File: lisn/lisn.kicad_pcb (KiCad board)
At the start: 2 copper layers, 50 x 49 mm, 33 parts, among them J1 IN+, J2 IN-, J3 GND, J4 GND, J5 OUT+, J6 OUT-, J7 SMA, SW1 DPDT, T1 SWB2010

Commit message: Update LISN PCB
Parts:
- added R9: 68, Resistor_SMD:R_0603_1608Metric, F.Cu at (160.6, 99.2)
- R5, R6: value 50 -> 82
- R7: value 18 -> 30
- R8: value 82 -> 68
- moved R8 27.1 mm to (164.7, 99.2)
- moved R3 4.33 mm to (167.3, 98.0)
- moved R4 4.33 mm to (168.8, 98.0)
- moved R1 2.55 mm to (156.5, 98.0)
- moved R2 2.55 mm to (158.0, 98.0)
- moved C4 2.50 mm to (160.5, 96.0), turned to -90 degrees
- moved C5 2.09 mm to (164.8, 96.0), turned to -90 degrees
- moved R7 1.43 mm to (137.8, 107.4)
- moved D1 1.10 mm to (158.7, 102.5)
- moved D2 1.04 mm to (161.1, 102.5)
- moved D3 0.99 mm to (163.5, 102.5)
- moved D4 0.94 mm to (165.9, 102.5)
- moved R5 0.10 mm to (154.1, 103.2)
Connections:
- R8 pad 1: GND -> Net-(D3-K)
- R8 pad 2: Net-(D5-A) -> GND
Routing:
- net GND: track 87.4 -> 134.3 mm
- net Net-(D3-K): track 18.9 -> 24.8 mm
- net Net-(D5-A): track 13.4 -> 10.3 mm
- net Net-(D1-K): track 16.4 -> 18.8 mm
- net Net-(C4-Pad2): track 5.27 -> 4.12 mm
- net /OUT_M: track 16.5 -> 17.6 mm
- net /OUTPUT: track 23.7 -> 24.6 mm

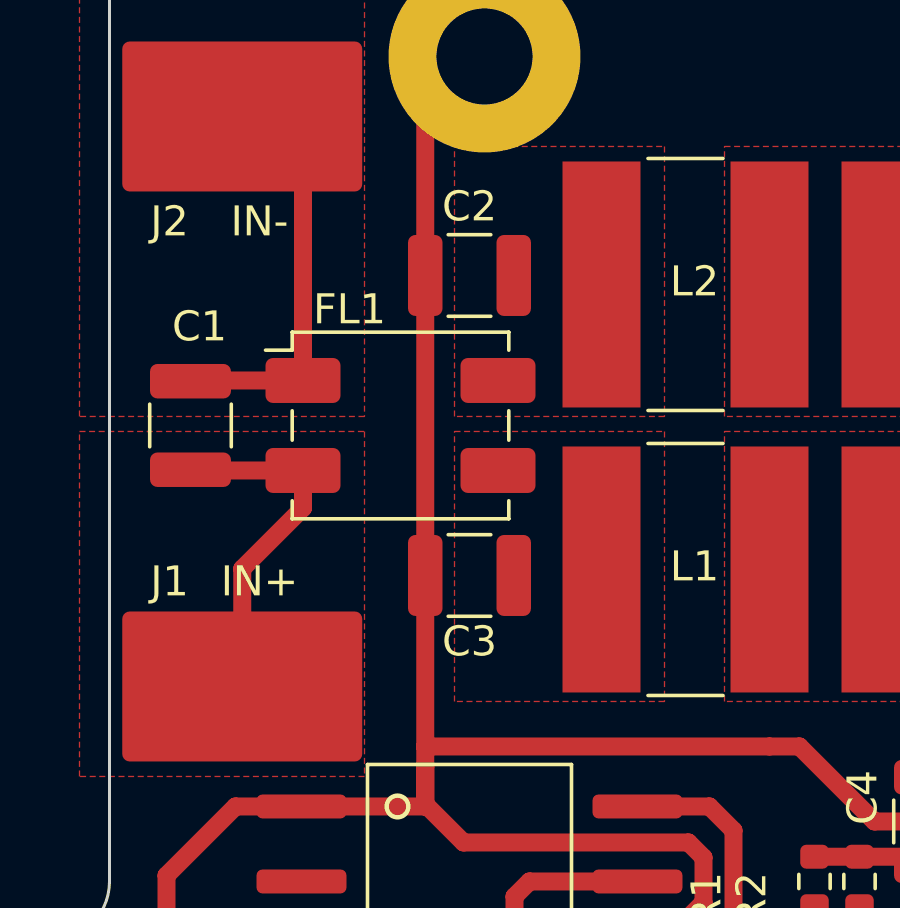
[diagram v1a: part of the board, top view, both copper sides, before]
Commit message: Add parametric FreeCAD design, add README.
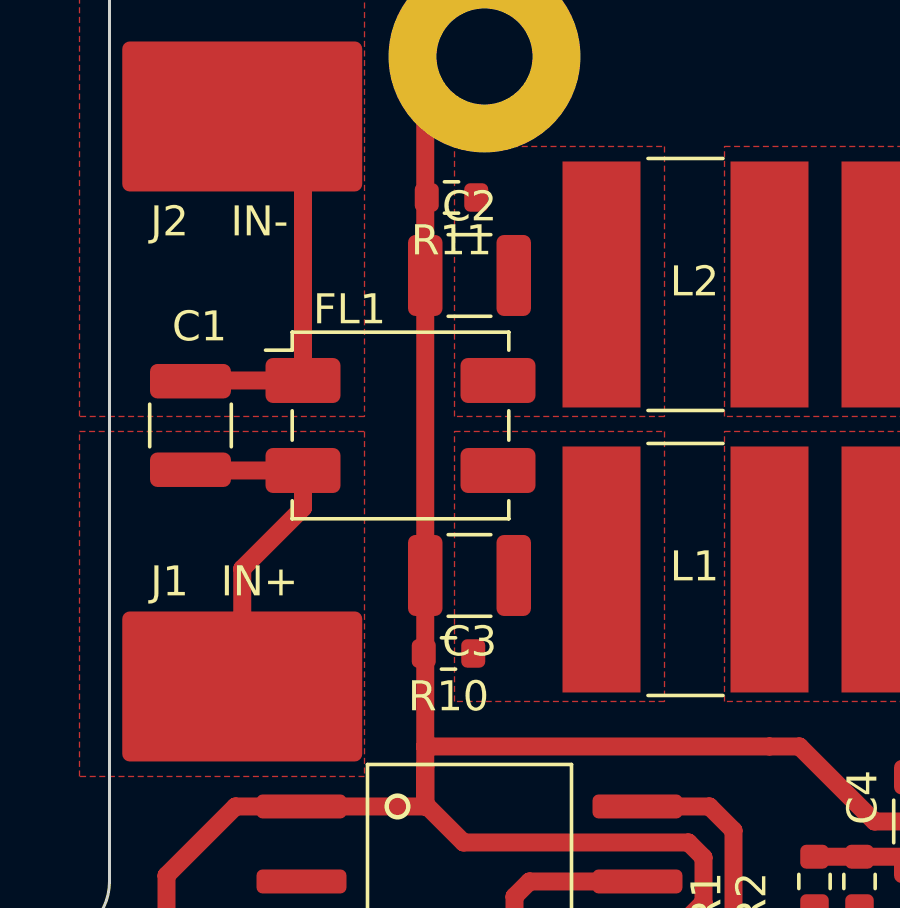
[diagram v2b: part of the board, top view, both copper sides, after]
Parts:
- added R10: 100k, Resistor_SMD:R_0603_1608Metric, F.Cu at (144.3, 90.4)
- added R11: 100k, Resistor_SMD:R_0603_1608Metric, F.Cu at (144.4, 75.2)
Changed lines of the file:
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@@
+  )
+  (footprint "Resistor_SMD:R_0603_1608Metric" (layer "F.Cu")
+    (at 144.3 90.4 180)
+    (descr "Resistor SMD 0603 (1608 Metric), square (rectangular) end terminal, IPC_7351 nominal, (Body size source: IPC-SM-782 page 72, https://www.pcb-3d.com/wordpress/wp-content/uploads/ipc-sm-782a_amendment_1_and_2.pdf), generated with kicad-footprint-generator")
+    (tags "resistor")
+    (property "Sheetfile" "lisn.kicad_sch")
+    (property "Sheetname" "")
+    (property "ki_description" "Resistor")
+    (property "ki_keywords" "R res resistor")
+    (attr smd)
+    (fp_text reference "R10" (at 0 -1.43) (layer "F.SilkS")
+        (effects (font (size 1 1) (thickness 0.15)))
+    )
+    (fp_text value "100k" (at 0 1.43) (layer "F.Fab")
+        (effects (font (size 1 1) (thickness 0.15)))
+    )
+    (fp_text user "${REFERENCE}" (at 0 0) (layer "F.Fab")
+        (effects (font (size 0.4 0.4) (thickness 0.06)))
+    )
+    (fp_line (start -0.237258 -0.5225) (end 0.237258 -0.5225)
+      (stroke (width 0.12) (type solid)) (layer "F.SilkS"))
+    (fp_line (start -0.237258 0.5225) (end 0.237258 0.5225)
+      (stroke (width 0.12) (type solid)) (layer "F.SilkS"))
+    (fp_line (start -1.48 -0.73) (end 1.48 -0.73)
+      (stroke (width 0.05) (type solid)) (layer "F.CrtYd"))
+    (fp_line (start -1.48 0.73) (end -1.48 -0.73)
+      (stroke (width 0.05) (type solid)) (layer "F.CrtYd"))
+    (fp_line (start 1.48 -0.73) (end 1.48 0.73)
+      (stroke (width 0.05) (type solid)) (layer "F.CrtYd"))
+    (fp_line (start 1.48 0.73) (end -1.48 0.73)
+      (stroke (width 0.05) (type solid)) (layer "F.CrtYd"))
+    (fp_line (start -0.8 -0.4125) (end 0.8 -0.4125)
+      (stroke (width 0.1) (type solid)) (layer "F.Fab"))
+    (fp_line (start -0.8 0.4125) (end -0.8 -0.4125)
+      (stroke (width 0.1) (type solid)) (layer "F.Fab"))
+    (fp_line (start 0.8 -0.4125) (end 0.8 0.4125)
+      (stroke (width 0.1) (type solid)) (layer "F.Fab"))
+    (fp_line (start 0.8 0.4125) (end -0.8 0.4125)
+      (stroke (width 0.1) (type solid)) (layer "F.Fab"))
+    (pad "1" smd roundrect (at -0.825 0 180) (size 0.8 0.95) (layers "F.Cu" "F.Paste" "F.Mask") (roundrect_rratio 0.25)
+      (net 5 "/INF_P") (pintype "passive"))
+    (pad "2" smd roundrect (at 0.825 0 180) (size 0.8 0.95) (layers "F.Cu" "F.Paste" "F.Mask") (roundrect_rratio 0.25)
+      (net 4 "GND") (pintype "passive"))
+    (model "${KICAD6_3DMODEL_DIR}/Resistor_SMD.3dshapes/R_0603_1608Metric.wrl"
+      (offset (xyz 0 0 0))
+      (scale (xyz 1 1 1))
+      (rotate (xyz 0 0 0))
+    )
   )
   (footprint "Resistor_SMD:R_0603_1608Metric" (layer "F.Cu")
@@
       (offset (xyz 0 0 0))
       (scale (xyz 1 1 1))
+      (rotate (xyz 0 0 0))
+    )
+  )
+  (footprint "Resistor_SMD:R_0603_1608Metric" (layer "F.Cu")
+    (at 144.4 75.2 180)
+    (descr "Resistor SMD 0603 (1608 Metric), square (rectangular) end terminal, IPC_7351 nominal, (Body size source: IPC-SM-782 page 72, https://www.pcb-3d.com/wordpress/wp-content/uploads/ipc-sm-782a_amendment_1_and_2.pdf), generated with kicad-footprint-generator")
+    (tags "resistor")
+    (property "Sheetfile" "lisn.kicad_sch")
+    (property "Sheetname" "")
+    (property "ki_description" "Resistor")
+    (property "ki_keywords" "R res resistor")
+    (attr smd)
+    (fp_text reference "R11" (at 0 -1.43) (layer "F.SilkS")
+        (effects (font (size 1 1) (thickness 0.15)))
+    )
+    (fp_text value "100k" (at 0 1.43) (layer "F.Fab")
+        (effects (font (size 1 1) (thickness 0.15)))
+    )
+    (fp_text user "${REFERENCE}" (at 0 0) (layer "F.Fab")
+        (effects (font (size 0.4 0.4) (thickness 0.06)))
+    )
+    (fp_line (start -0.237258 -0.5225) (end 0.237258 -0.5225)
+      (stroke (width 0.12) (type solid)) (layer "F.SilkS"))
+    (fp_line (start -0.237258 0.5225) (end 0.237258 0.5225)
+      (stroke (width 0.12) (type solid)) (layer "F.SilkS"))
+    (fp_line (start -1.48 -0.73) (end 1.48 -0.73)
+      (stroke (width 0.05) (type solid)) (layer "F.CrtYd"))
+    (fp_line (start -1.48 0.73) (end -1.48 -0.73)
+      (stroke (width 0.05) (type solid)) (layer "F.CrtYd"))
+    (fp_line (start 1.48 -0.73) (end 1.48 0.73)
+      (stroke (width 0.05) (type solid)) (layer "F.CrtYd"))
+    (fp_line (start 1.48 0.73) (end -1.48 0.73)
+      (stroke (width 0.05) (type solid)) (layer "F.CrtYd"))
+    (fp_line (start -0.8 -0.4125) (end 0.8 -0.4125)
+      (stroke (width 0.1) (type solid)) (layer "F.Fab"))
+    (fp_line (start -0.8 0.4125) (end -0.8 -0.4125)
+      (stroke (width 0.1) (type solid)) (layer "F.Fab"))
+    (fp_line (start 0.8 -0.4125) (end 0.8 0.4125)
+      (stroke (width 0.1) (type solid)) (layer "F.Fab"))
+    (fp_line (start 0.8 0.4125) (end -0.8 0.4125)
+      (stroke (width 0.1) (type solid)) (layer "F.Fab"))
+    (pad "1" smd roundrect (at -0.825 0 180) (size 0.8 0.95) (layers "F.Cu" "F.Paste" "F.Mask") (roundrect_rratio 0.25)
+      (net 3 "/INF_M") (pintype "passive"))
+    (pad "2" smd roundrect (at 0.825 0 180) (size 0.8 0.95) (layers "F.Cu" "F.Paste" "F.Mask") (roundrect_rratio 0.25)
+      (net 4 "GND") (pintype "passive"))
+    (model "${KICAD6_3DMODEL_DIR}/Resistor_SMD.3dshapes/R_0603_1608Metric.wrl"
+      (offset (xyz 0 0 0))
+      (scale (xyz 1 1 1))
